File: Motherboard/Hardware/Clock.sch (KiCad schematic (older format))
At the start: 11 parts, among them Q1 BC848, Q47 BC848, Q48 BC858, Q49 BC848

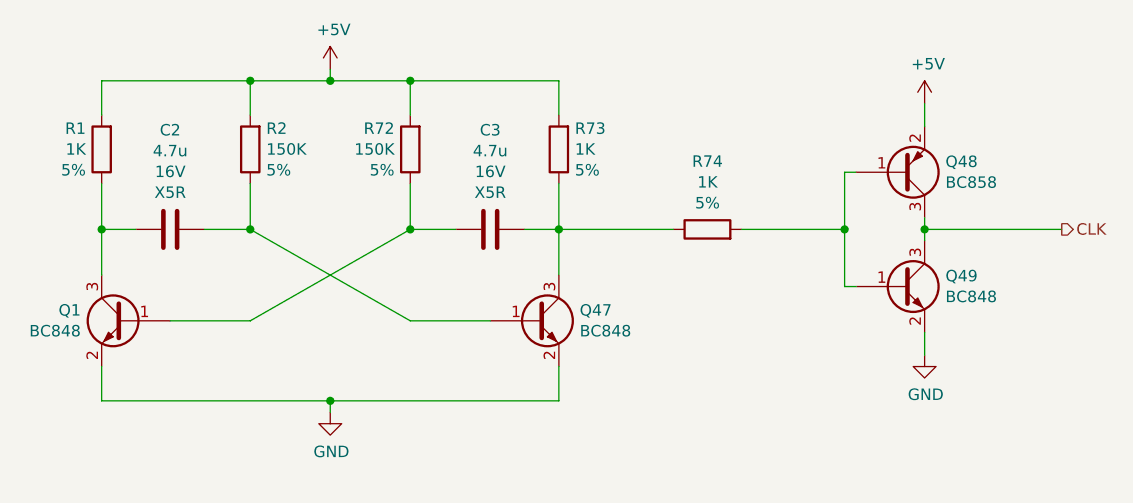
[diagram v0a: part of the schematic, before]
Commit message: Renamed all motherboard components so the name are ordered.
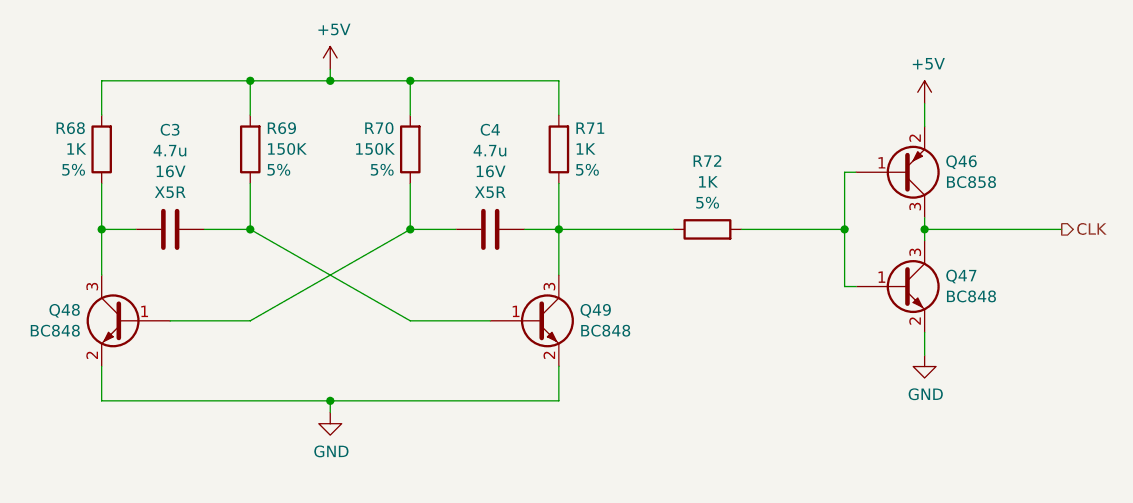
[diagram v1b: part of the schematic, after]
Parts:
- renumbered C2 to C3, C3 to C4, Q48 to Q46, Q49 to Q47, Q1 to Q48, Q47 to Q49, R1 to R68, R2 to R69, R72 to R70, R73 to R71, R74 to R72
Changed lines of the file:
@@
 AR Path="/622D8B2C" Ref="Q?"  Part="1"
 AR Path="/61D90E9A/622D8B2C" Ref="Q?"  Part="1"
-AR Path="/622B55AD/622D8B2C" Ref="Q47"  Part="1"
-F 0 "Q47" H 6041 3746 50  0000 L CNN
+AR Path="/622B55AD/622D8B2C" Ref="Q49"  Part="1"
+F 0 "Q49" H 6041 3746 50  0000 L CNN
 F 1 "BC848" H 6041 3655 50  0000 L CNN
 F 2 "Package_TO_SOT_SMD:SOT-23" H 6050 3625 50  0001 L CIN
@@
 AR Path="/622E2085" Ref="R?"  Part="1"
 AR Path="/61D90E9A/622E2085" Ref="R?"  Part="1"
-AR Path="/622B55AD/622E2085" Ref="R73"  Part="1"
-F 0 "R73" H 5880 2859 50  0000 R CNN
+AR Path="/622B55AD/622E2085" Ref="R71"  Part="1"
+F 0 "R71" H 5880 2859 50  0000 R CNN
 F 1 "1K" H 5880 2950 50  0000 R CNN
 F 2 "Resistor_SMD:R_0603_1608Metric_Pad0.98x0.95mm_HandSolder" V 5880 2950 50  0001 C CNN
@@
 P 5650 3300
 AR Path="/61D90E9A/622E208F" Ref="C?"  Part="1"
-AR Path="/622B55AD/622E208F" Ref="C3"  Part="1"
-F 0 "C3" V 5216 3300 50  0000 C CNN
+AR Path="/622B55AD/622E208F" Ref="C4"  Part="1"
+F 0 "C4" V 5216 3300 50  0000 C CNN
 F 1 "4.7u" V 5307 3300 50  0000 C CNN
 F 2 "Capacitor_SMD:C_0805_2012Metric_Pad1.18x1.45mm_HandSolder" H 5688 3150 50  0001 C CNN
@@
 P 4950 4100
 AR Path="/61D90E9A/622E20A3" Ref="#PWR?"  Part="1"
-AR Path="/622B55AD/622E20A3" Ref="#PWR02"  Part="1"
-F 0 "#PWR02" H 4950 3850 50  0001 C CNN
+AR Path="/622B55AD/622E20A3" Ref="#PWR062"  Part="1"
+F 0 "#PWR062" H 4950 3850 50  0001 C CNN
 F 1 "GND" H 4955 3927 50  0000 C CNN
 F 2 "" H 4950 4100 50  0001 C CNN
@@
 AR Path="/622EE2C1" Ref="R?"  Part="1"
 AR Path="/61D90E9A/622EE2C1" Ref="R?"  Part="1"
-AR Path="/622B55AD/622EE2C1" Ref="R72"  Part="1"
-F 0 "R72" H 5369 2859 50  0000 L CNN
+AR Path="/622B55AD/622EE2C1" Ref="R70"  Part="1"
+F 0 "R70" H 5369 2859 50  0000 L CNN
 F 1 "150K" H 5369 2950 50  0000 L CNN
 F 2 "Resistor_SMD:R_0603_1608Metric_Pad0.98x0.95mm_HandSolder" V 5230 2950 50  0001 C CNN
@@
 AR Path="/622F0556" Ref="R?"  Part="1"
 AR Path="/61D90E9A/622F0556" Ref="R?"  Part="1"
-AR Path="/622B55AD/622F0556" Ref="R2"  Part="1"
-F 0 "R2" H 4530 2859 50  0000 R CNN
+AR Path="/622B55AD/622F0556" Ref="R69"  Part="1"
+F 0 "R69" H 4530 2859 50  0000 R CNN
 F 1 "150K" H 4530 2950 50  0000 R CNN
 F 2 "Resistor_SMD:R_0603_1608Metric_Pad0.98x0.95mm_HandSolder" V 4530 2950 50  0001 C CNN
@@
 P 4250 3300
 AR Path="/61D90E9A/622F0560" Ref="C?"  Part="1"
-AR Path="/622B55AD/622F0560" Ref="C2"  Part="1"
-F 0 "C2" V 3816 3300 50  0000 C CNN
+AR Path="/622B55AD/622F0560" Ref="C3"  Part="1"
+F 0 "C3" V 3816 3300 50  0000 C CNN
 F 1 "4.7u" V 3907 3300 50  0000 C CNN
 F 2 "Capacitor_SMD:C_0805_2012Metric_Pad1.18x1.45mm_HandSolder" H 4288 3150 50  0001 C CNN
@@
 AR Path="/622F056A" Ref="R?"  Part="1"
 AR Path="/61D90E9A/622F056A" Ref="R?"  Part="1"
-AR Path="/622B55AD/622F056A" Ref="R1"  Part="1"
-F 0 "R1" H 4019 2859 50  0000 L CNN
+AR Path="/622B55AD/622F056A" Ref="R68"  Part="1"
+F 0 "R68" H 4019 2859 50  0000 L CNN
 F 1 "1K" H 4019 2950 50  0000 L CNN
 F 2 "Resistor_SMD:R_0603_1608Metric_Pad0.98x0.95mm_HandSolder" V 3880 2950 50  0001 C CNN
@@
 AR Path="/622F1973" Ref="Q?"  Part="1"
 AR Path="/61D90E9A/622F1973" Ref="Q?"  Part="1"
-AR Path="/622B55AD/622F1973" Ref="Q1"  Part="1"
-F 0 "Q1" H 4241 3746 50  0000 L CNN
+AR Path="/622B55AD/622F1973" Ref="Q48"  Part="1"
+F 0 "Q48" H 4241 3746 50  0000 L CNN
 F 1 "BC848" H 4241 3655 50  0000 L CNN
 F 2 "Package_TO_SOT_SMD:SOT-23" H 4250 3625 50  0001 L CIN
@@
 AR Path="/622E209C" Ref="#PWR?"  Part="1"
 AR Path="/61D90E9A/622E209C" Ref="#PWR?"  Part="1"
-AR Path="/622B55AD/622E209C" Ref="#PWR01"  Part="1"
-F 0 "#PWR01" H 4950 2450 50  0001 C CNN
+AR Path="/622B55AD/622E209C" Ref="#PWR059"  Part="1"
+F 0 "#PWR059" H 4950 2450 50  0001 C CNN
 F 1 "+5V" H 4965 2773 50  0000 C CNN
 F 2 "" H 4950 2600 50  0001 C CNN
@@
 AR Path="/6231F3AD" Ref="Q?"  Part="1"
 AR Path="/61D90E9A/6231F3AD" Ref="Q?"  Part="1"
-AR Path="/622B55AD/6231F3AD" Ref="Q49"  Part="1"
-F 0 "Q49" H 7641 3596 50  0000 L CNN
+AR Path="/622B55AD/6231F3AD" Ref="Q47"  Part="1"
+F 0 "Q47" H 7641 3596 50  0000 L CNN
 F 1 "BC848" H 7641 3505 50  0000 L CNN
 F 2 "Package_TO_SOT_SMD:SOT-23" H 7650 3475 50  0001 L CIN
@@
 P 7450 3050
 AR Path="/61D90E9A/62322225" Ref="Q?"  Part="1"
-AR Path="/622B55AD/62322225" Ref="Q48"  Part="1"
-F 0 "Q48" H 7641 3004 50  0000 L CNN
+AR Path="/622B55AD/62322225" Ref="Q46"  Part="1"
+F 0 "Q46" H 7641 3004 50  0000 L CNN
 F 1 "BC858" H 7641 3095 50  0000 L CNN
 F 2 "Package_TO_SOT_SMD:SOT-23" H 7650 2975 50  0001 L CIN
@@
 AR Path="/6232222E" Ref="#PWR?"  Part="1"
 AR Path="/61D90E9A/6232222E" Ref="#PWR?"  Part="1"
-AR Path="/622B55AD/6232222E" Ref="#PWR03"  Part="1"
-F 0 "#PWR03" H 7550 2600 50  0001 C CNN
+AR Path="/622B55AD/6232222E" Ref="#PWR060"  Part="1"
+F 0 "#PWR060" H 7550 2600 50  0001 C CNN
 F 1 "+5V" H 7565 2923 50  0000 C CNN
 F 2 "" H 7550 2750 50  0001 C CNN
@@
 P 7550 3850
 AR Path="/61D90E9A/623234BD" Ref="#PWR?"  Part="1"
-AR Path="/622B55AD/623234BD" Ref="#PWR04"  Part="1"
-F 0 "#PWR04" H 7550 3600 50  0001 C CNN
+AR Path="/622B55AD/623234BD" Ref="#PWR061"  Part="1"
+F 0 "#PWR061" H 7550 3600 50  0001 C CNN
 F 1 "GND" H 7555 3677 50  0000 C CNN
 F 2 "" H 7550 3850 50  0001 C CNN
@@
 AR Path="/62329898" Ref="R?"  Part="1"
 AR Path="/61D90E9A/62329898" Ref="R?"  Part="1"
-AR Path="/622B55AD/62329898" Ref="R74"  Part="1"
-F 0 "R74" V 6897 3300 50  0000 C CNN
+AR Path="/622B55AD/62329898" Ref="R72"  Part="1"
+F 0 "R72" V 6897 3300 50  0000 C CNN
 F 1 "1K" V 6806 3300 50  0000 C CNN
 F 2 "Resistor_SMD:R_0603_1608Metric_Pad0.98x0.95mm_HandSolder" V 6530 3300 50  0001 C CNN

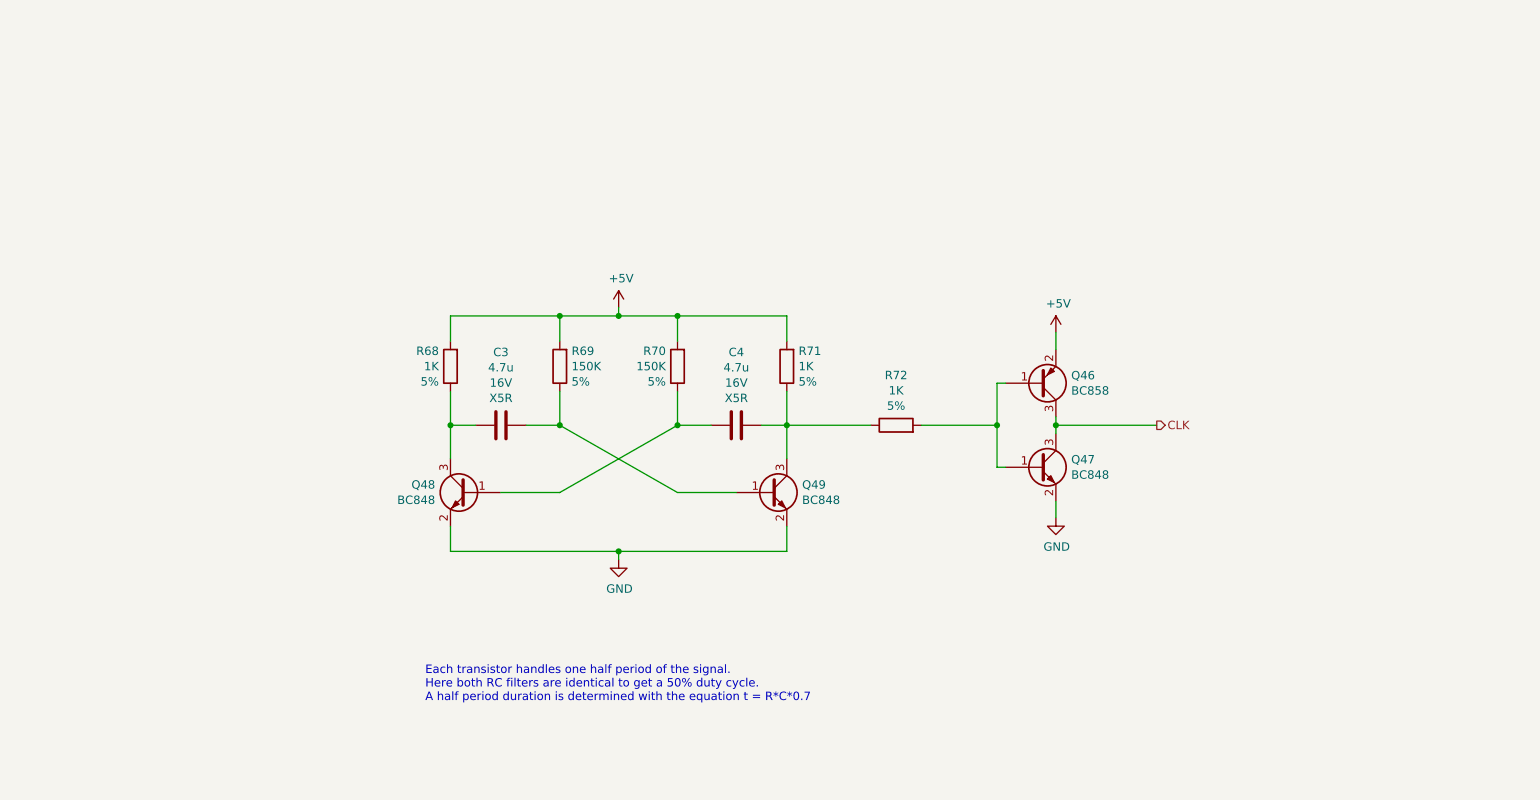
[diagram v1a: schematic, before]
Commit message: Disabled the motherboard clock circuit power supply while power-on reset delay is running to avoid clocking the RS gates while they are being reset by the power-on reset.
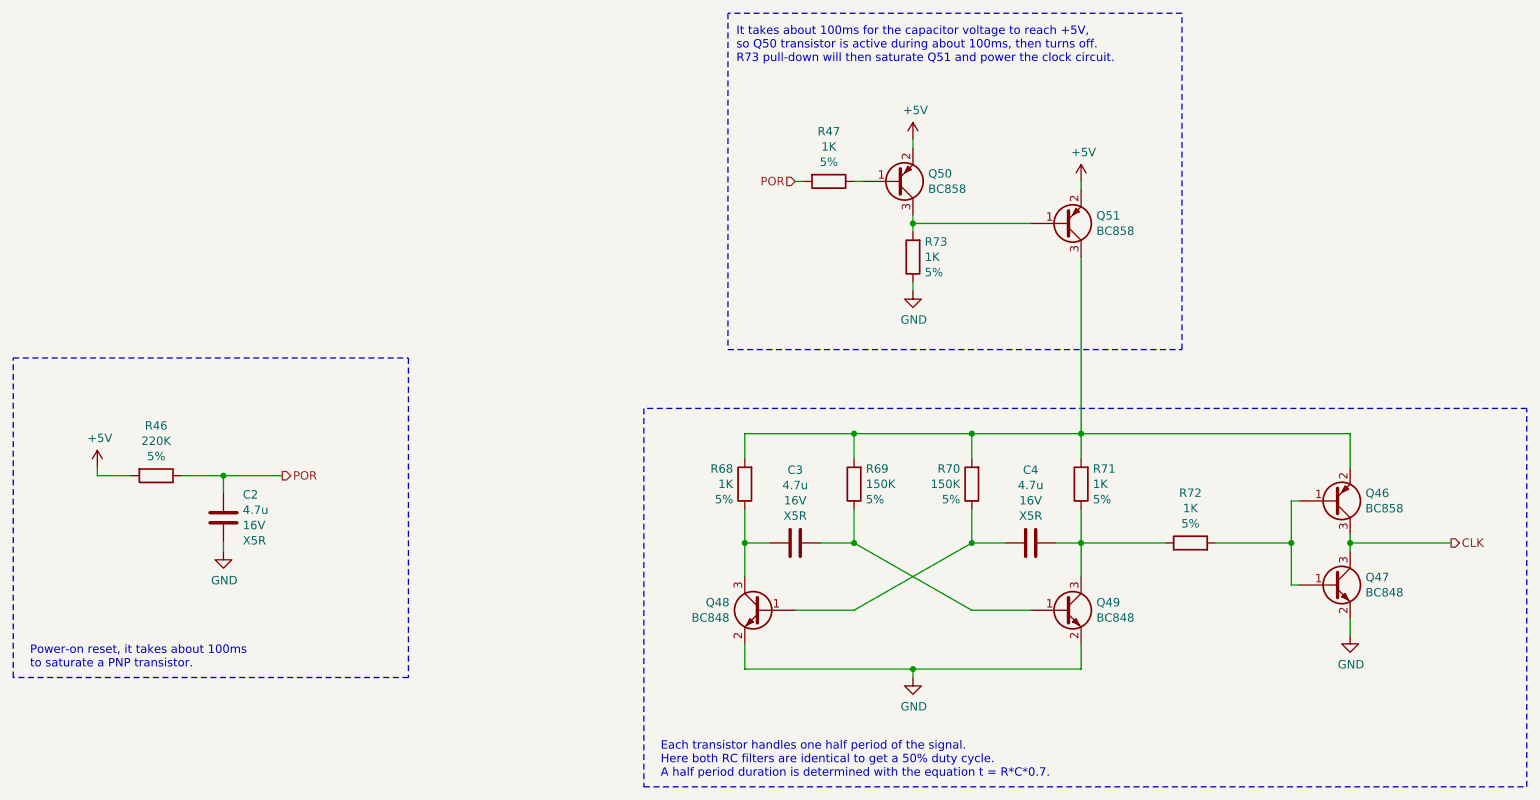
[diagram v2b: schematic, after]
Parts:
- added C2: 4.7u, Capacitor_SMD:C_0805_2012Metric_Pad1.18x1.45mm_HandSolder, symbol Device:C
- added Q50, Q51: BC858, Package_TO_SOT_SMD:SOT-23, symbol Transistor_BJT:BC858
- added R46: 220K, Resistor_SMD:R_0603_1608Metric_Pad0.98x0.95mm_HandSolder, symbol Device:R
- added R47, R73: 1K, Resistor_SMD:R_0603_1608Metric_Pad0.98x0.95mm_HandSolder, symbol Device:R
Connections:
- net +5V: now also Q50.2 (E), Q51.2 (E), R46.2; no longer Q46.2 (E), R68.2, R69.2, R70.2, R71.2
- net GND: now also C2.2, R73.1
- new net: Q50.1 (B), R47.1
- new net: Q50.3 (C), Q51.1 (B), R73.2
- new net: Q46.2 (E), Q51.3 (C), R68.2, R69.2, R70.2, R71.2
- new net POR: C2.1, R46.1, R47.2
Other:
- note added: "Each transistor handles one half period of the signal.\nHere both RC filters are identical to get a 50% duty cycle.\nA half period duration is determined with the equation t = R*C*0.7."
- note added: "It takes about 100ms for the capacitor voltage to reach +5V,\nso Q50 transistor is active during about 100ms, then turns off.\nR73 pull-down will then saturate Q51 and power the clock circuit."
- note added: "Power-on reset, it takes about 100ms\nto saturate a PNP transistor."
- note removed: "Each transistor handles one half period of the signal.\nHere both RC filters are identical to get a 50% duty cycle.\nA half period duration is determined with the equation t = R*C*0.7"
- moved on the sheet: C3, C4, Q46, Q47, Q48, Q49, R68, R69, R70, R71, R72

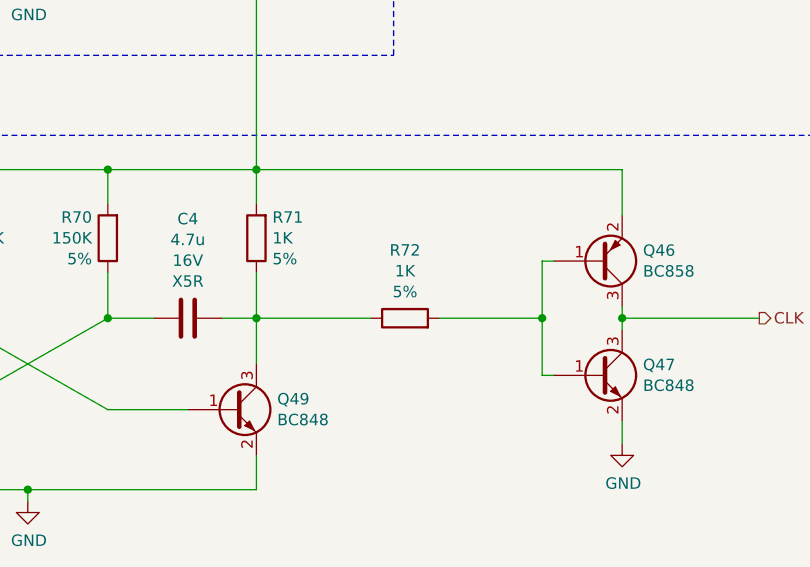
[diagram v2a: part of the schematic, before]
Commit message: Fixed clock output push-pull stage in schematic.
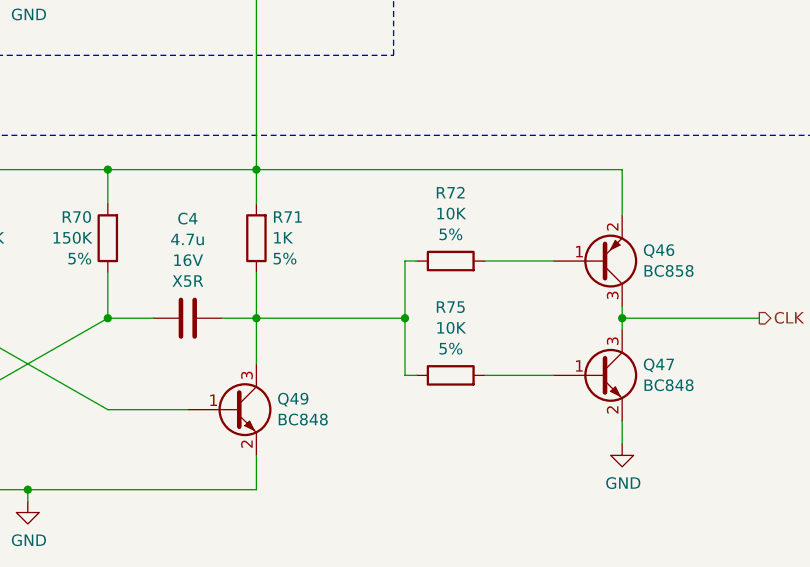
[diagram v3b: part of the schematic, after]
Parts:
- added R75: 10K, Resistor_SMD:R_0603_1608Metric_Pad0.98x0.95mm_HandSolder, symbol Device:R
- R72: value 1K -> 10K
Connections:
- net at C4.1, Q49.3 (C), R71.1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: now also R75.1
- net at Q46.1 (B), R72.2: no longer Q47.1 (B)
- new net: Q47.1 (B), R75.2
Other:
- moved on the sheet: R72
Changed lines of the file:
@@
 Wire Wire Line
 	7700 3800 7700 4000
-Wire Wire Line
-	7550 4000 7700 4000
 Connection ~ 7700 4000
 Wire Wire Line
@@
 L Device:R R?
 U 1 1 62329898
-P 8350 4000
+P 8550 3750
 AR Path="/62329898" Ref="R?"  Part="1"
 AR Path="/61D90E9A/62329898" Ref="R?"  Part="1"
 AR Path="/622B55AD/62329898" Ref="R72"  Part="1"
-F 0 "R72" V 8647 4000 50  0000 C CNN
-F 1 "1K" V 8556 4000 50  0000 C CNN
-F 2 "Resistor_SMD:R_0603_1608Metric_Pad0.98x0.95mm_HandSolder" V 8280 4000 50  0001 C CNN
-F 3 "~" H 8350 4000 50  0001 C CNN
-F 4 "5%" V 8465 4000 50  0000 C CNN "Value2"
-F 5 "R" H 8350 4000 50  0001 C CNN "Spice_Primitive"
-F 6 "1k" H 8350 4000 50  0001 C CNN "Spice_Model"
-F 7 "Y" H 8350 4000 50  0001 C CNN "Spice_Netlist_Enabled"
-	1    8350 4000
+F 0 "R72" V 8847 3750 50  0000 C CNN
+F 1 "10K" V 8756 3750 50  0000 C CNN
+F 2 "Resistor_SMD:R_0603_1608Metric_Pad0.98x0.95mm_HandSolder" V 8480 3750 50  0001 C CNN
+F 3 "~" H 8550 3750 50  0001 C CNN
+F 4 "5%" V 8665 3750 50  0000 C CNN "Value2"
+F 5 "R" H 8550 3750 50  0001 C CNN "Spice_Primitive"
+F 6 "1k" H 8550 3750 50  0001 C CNN "Spice_Model"
+F 7 "Y" H 8550 3750 50  0001 C CNN "Spice_Netlist_Enabled"
+	1    8550 3750
 	0    -1   -1   0
 $EndComp
-Wire Wire Line
-	9000 3750 8950 3750
-Wire Wire Line
-	8950 3750 8950 4000
-Wire Wire Line
-	8950 4000 8500 4000
-Wire Wire Line
-	8950 4000 8950 4250
-Wire Wire Line
-	8950 4250 9000 4250
-Connection ~ 8950 4000
-Wire Wire Line
-	7700 4000 8200 4000
 Text HLabel 9900 4000 2    50   Output ~ 0
 CLK
@@
 Wire Notes Line
 	10350 3200 5100 3200
+$Comp
+L Device:R R?
+U 1 1 623800AC
+P 8550 4250
+AR Path="/623800AC" Ref="R?"  Part="1"
+AR Path="/61D90E9A/623800AC" Ref="R?"  Part="1"
+AR Path="/622B55AD/623800AC" Ref="R75"  Part="1"
+F 0 "R75" V 8847 4250 50  0000 C CNN
+F 1 "10K" V 8756 4250 50  0000 C CNN
+F 2 "Resistor_SMD:R_0603_1608Metric_Pad0.98x0.95mm_HandSolder" V 8480 4250 50  0001 C CNN
+F 3 "~" H 8550 4250 50  0001 C CNN
+F 4 "5%" V 8665 4250 50  0000 C CNN "Value2"
+F 5 "R" H 8550 4250 50  0001 C CNN "Spice_Primitive"
+F 6 "1k" H 8550 4250 50  0001 C CNN "Spice_Model"
+F 7 "Y" H 8550 4250 50  0001 C CNN "Spice_Netlist_Enabled"
+	1    8550 4250
+	0    -1   -1   0
+$EndComp
+Wire Wire Line
+	8350 4000 8350 3750
+Wire Wire Line
+	8350 3750 8400 3750
+Wire Wire Line
+	7700 4000 8350 4000
+Wire Wire Line
+	7550 4000 7700 4000
+Wire Wire Line
+	8350 4000 8350 4250
+Wire Wire Line
+	8350 4250 8400 4250
+Connection ~ 8350 4000
+Wire Wire Line
+	8700 3750 9000 3750
+Wire Wire Line
+	8700 4250 9000 4250
 $EndSCHEMATC
